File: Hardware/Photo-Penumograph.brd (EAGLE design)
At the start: 51.5 x 56.1 mm, 49 parts, among them SW1 SWITCH.JS202011JCQN

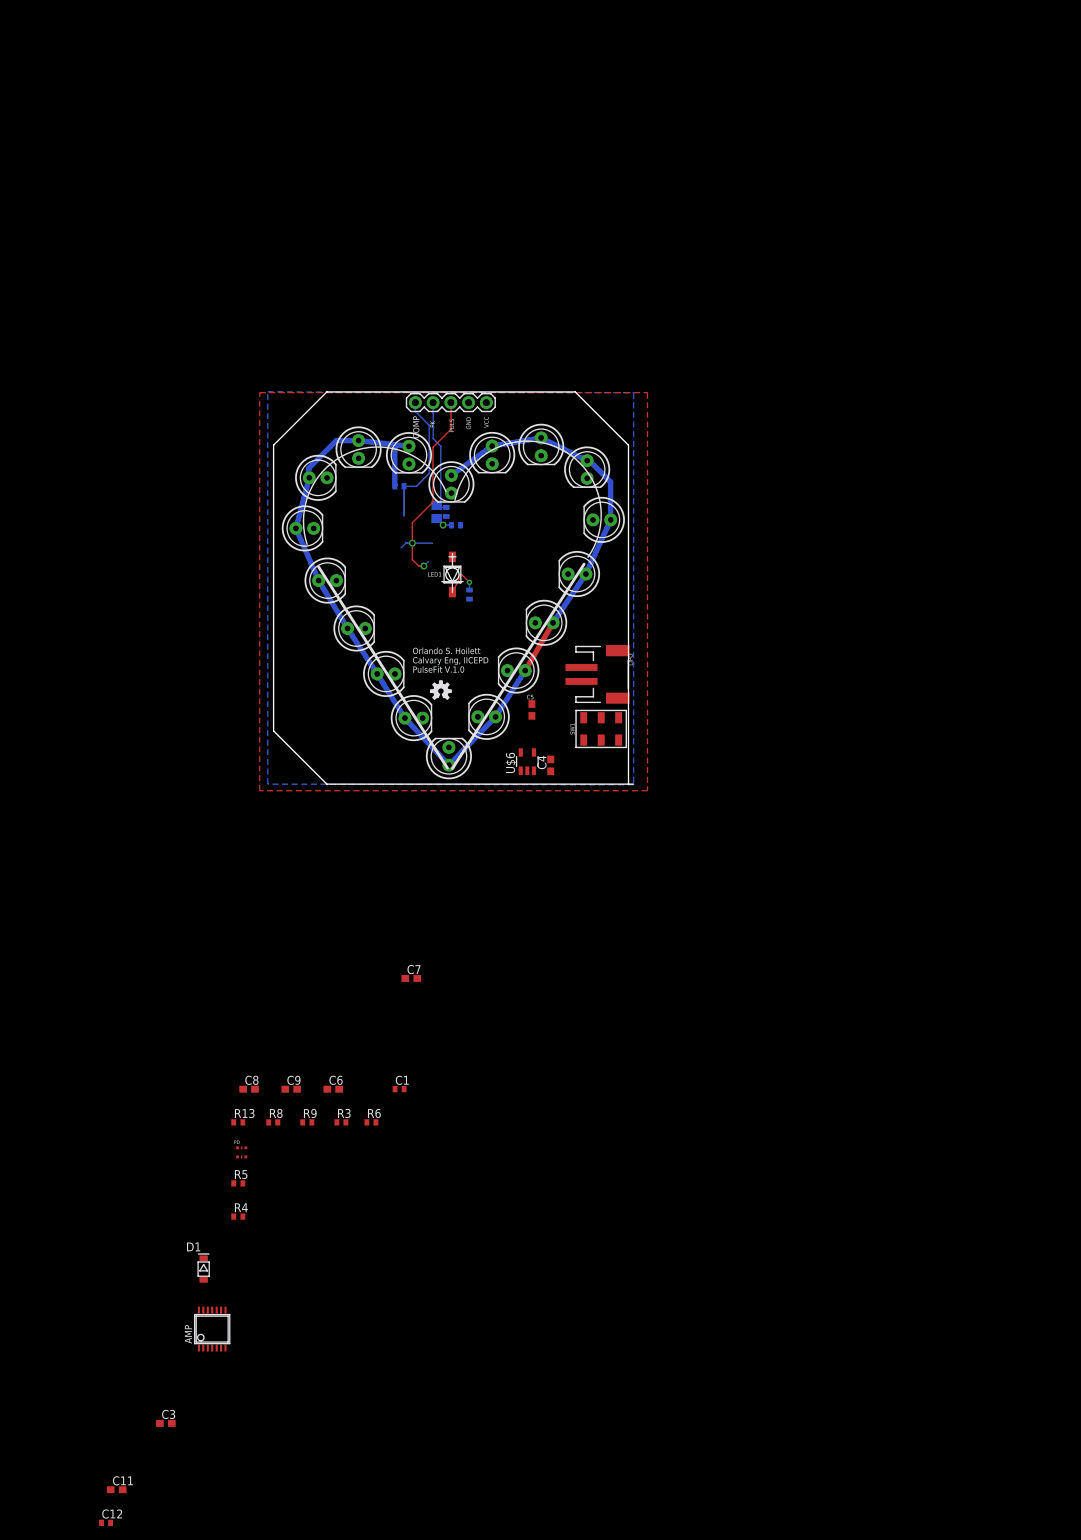
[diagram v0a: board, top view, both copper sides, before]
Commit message: Inital lung idea, doesn't expand with breath.
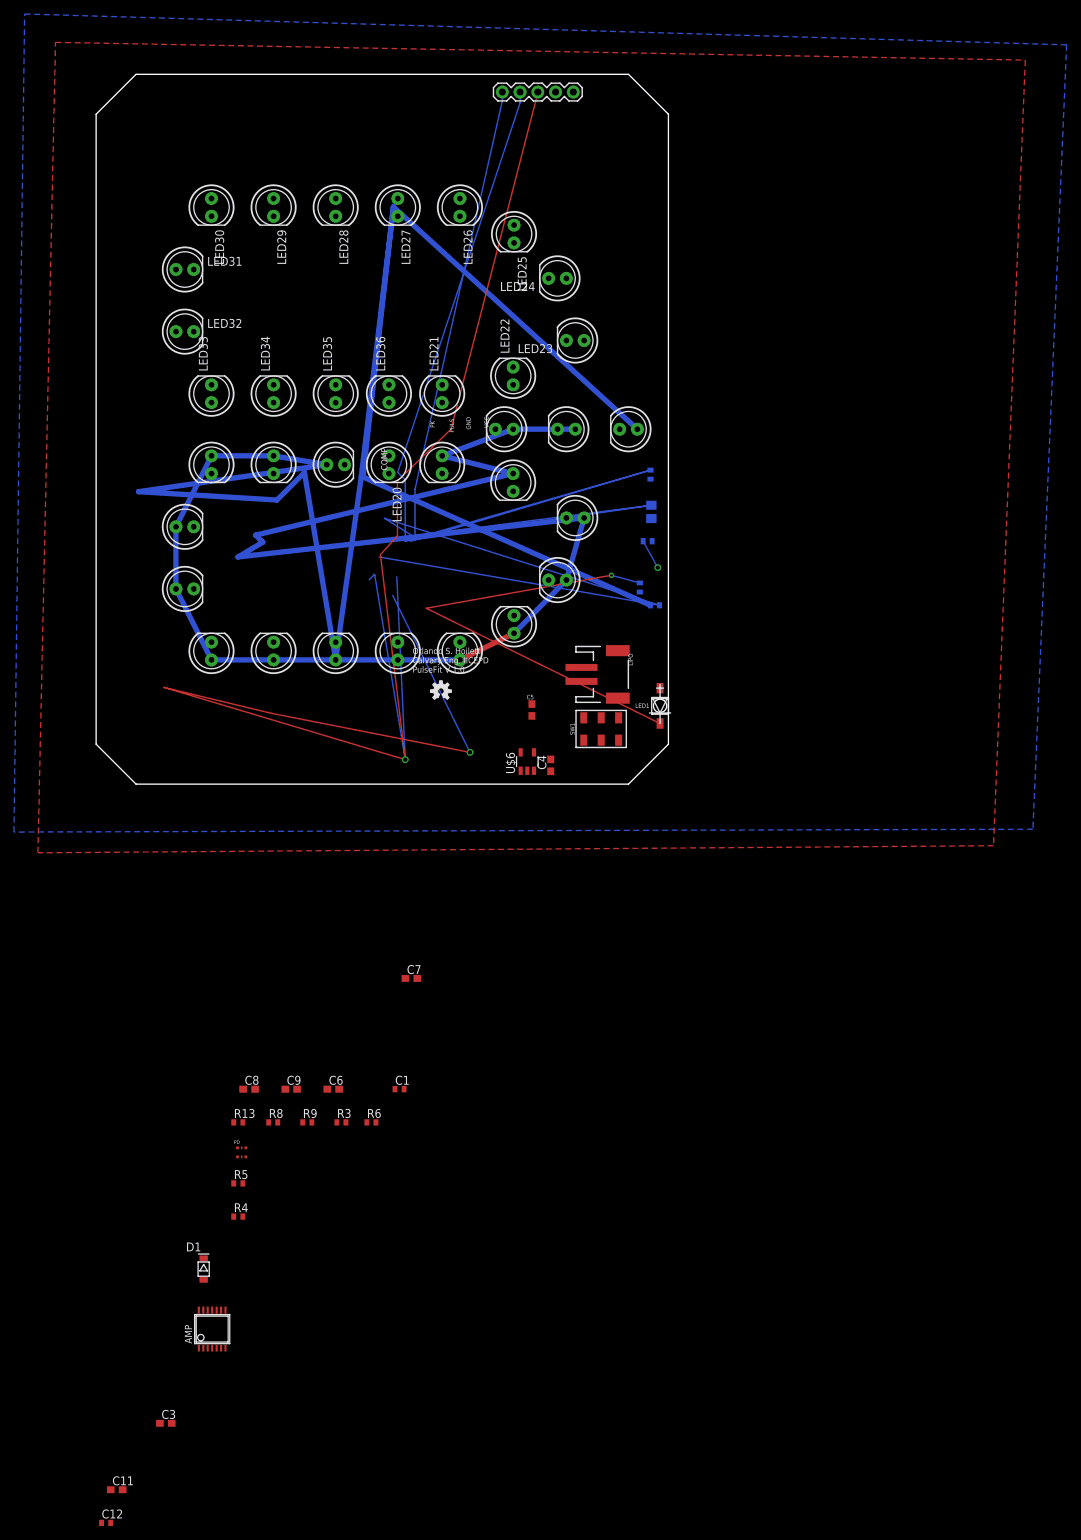
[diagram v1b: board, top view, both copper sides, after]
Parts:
- added LED20, LED21, LED22, LED23, LED24, LED25, LED26, LED27, LED28, LED29, LED30, LED31, LED32, LED33, LED34, LED35, LED36: (no value), SparkFun-LED:LED5MM
- moved BREAKOUT 46.2 mm to (58.1, 99.1)
- moved R1 40.3 mm to (80.0, 25.6)
- moved LED1 35.2 mm to (80.7, 11.2)
- moved LED19 31.6 mm to (76.2, 50.8), turned to 180 degrees
- moved LED13 31.3 mm to (12.7, 27.9)
- moved C10 30.7 mm to (79.5, 39.0)
- moved LED12 30.5 mm to (16.5, 19.1), turned to 90 degrees
- moved R12 29.7 mm to (79.3, 44.3)
- moved LED11 29.3 mm to (25.4, 19.1)
- moved LED18 29.0 mm to (34.3, 19.1), turned to 90 degrees
- moved LED14 28.6 mm to (12.7, 36.8)
- moved C2 27.5 mm to (78.9, 34.8)
- moved R2 24.4 mm to (77.8, 28.1)
- moved LED15 23.5 mm to (16.5, 45.7), turned to 270 degrees
- moved LED2 18.2 mm to (67.3, 50.8), turned to 180 degrees
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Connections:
- net ANODE: now also LED20.A, LED21.A, LED22.A, LED23.A, LED24.A, LED25.A, LED26.A, LED27.A, LED28.A, LED29.A, LED30.A, LED32.A, LED33.A, LED34.A, LED35.A, LED36.A
- net GND: now also LED20.K, LED21.K, LED22.K, LED23.K, LED24.K, LED25.K, LED26.K, LED27.K, LED28.K, LED29.K, LED30.K, LED31.K, LED32.K, LED33.K, LED34.K, LED35.K, LED36.K
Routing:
- net ANODE: track 145.5 -> 512.3 mm
- net PULSE: track 32.6 -> 261.7 mm
- net PEAK: track 17.5 -> 212.1 mm
- net COMP: track 19.6 -> 152.3 mm
- net N$9: track 5.54 -> 68.5 mm
- net 3.3V: track 1.20 -> 4.33 mm
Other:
- board size 51.5 x 56.1 mm -> 81.9 x 101.6 mm

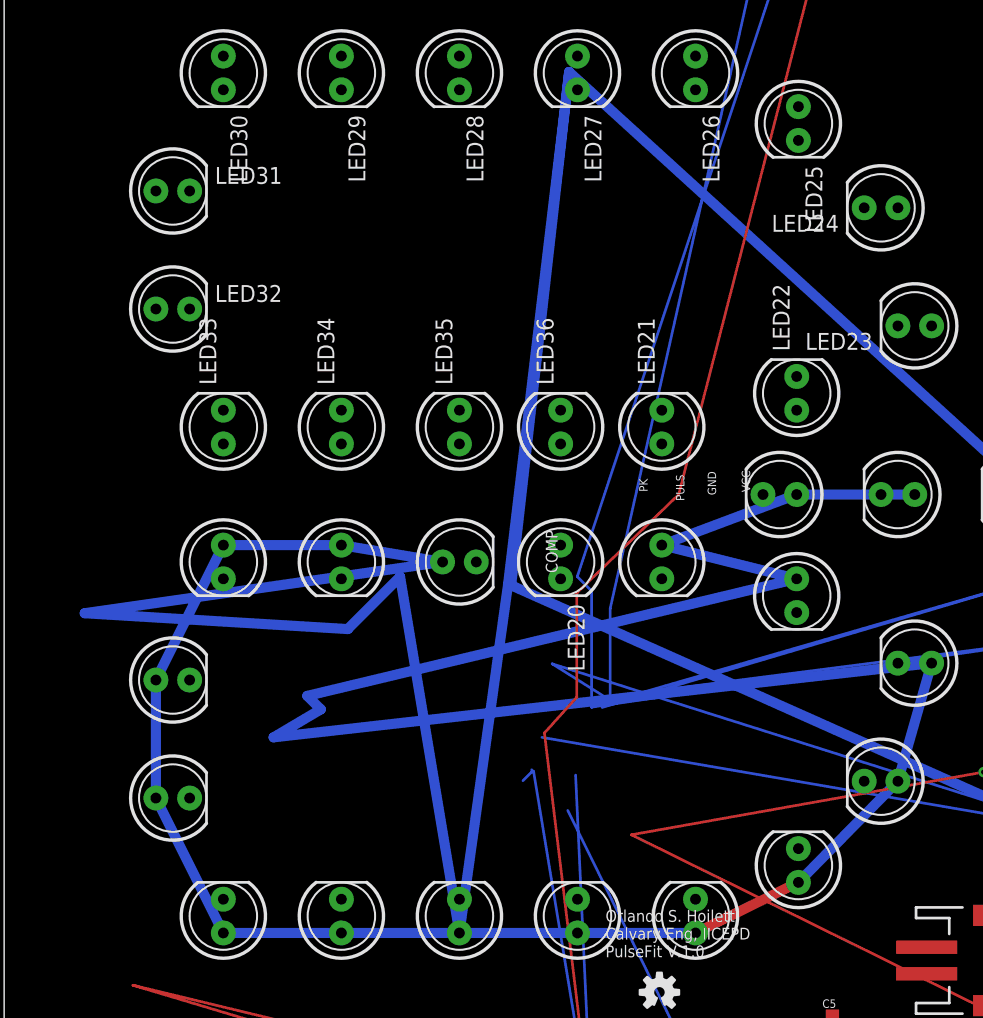
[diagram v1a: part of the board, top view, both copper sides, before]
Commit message: Improved basic lung design
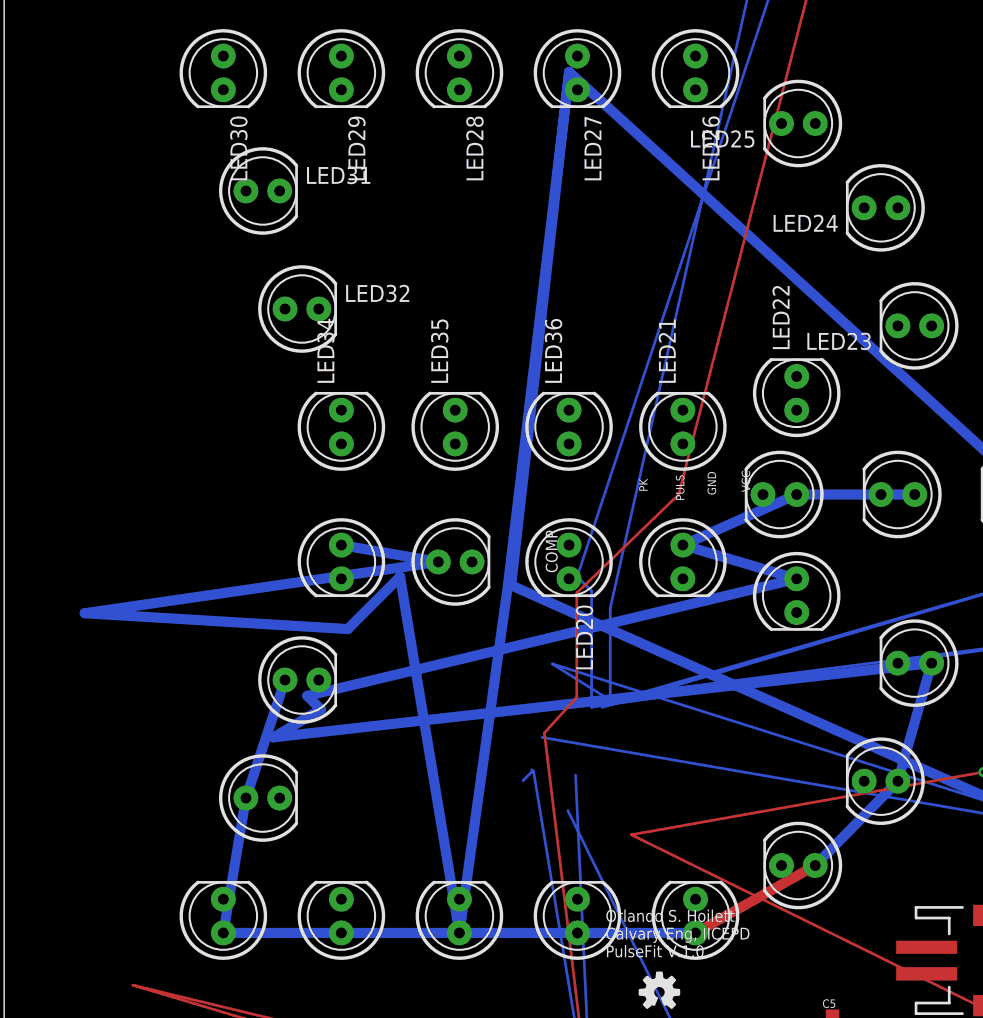
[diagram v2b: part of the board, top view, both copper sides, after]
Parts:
- removed LED15, LED33: (no value), SparkFun-LED:LED5MM
- moved LED14 9.73 mm to (22.4, 36.8)
- moved LED32 9.73 mm to (22.4, 64.8)
- moved LED13 6.78 mm to (19.5, 27.9)
- moved LED31 6.78 mm to (19.5, 73.7)
- moved LED21 1.59 mm to (51.1, 55.9)
- moved LED4 1.59 mm to (51.1, 45.7)
- moved LED20 0.64 mm to (42.5, 45.7)
- moved LED36 0.64 mm to (42.5, 55.9)
- moved LED17 0.32 mm to (34.0, 45.7)
- moved LED35 0.32 mm to (34.0, 55.9)
- turned LED25 to 180 degrees
- turned LED8 to 180 degrees
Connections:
- net ANODE: no longer LED15.A, LED33.A
- net GND: no longer LED15.K, LED33.K
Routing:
- net ANODE: track 512.3 -> 487.8 mm
